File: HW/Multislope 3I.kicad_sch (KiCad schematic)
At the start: 126 parts, among them J1 INT, J10 PWR, J11 TEST, J12 UART, J13 INPUT, J14 SLOPE, J15 PWR, J2 TEST, J3 COMP, J4 SLOT, J5 SLOT, J6 SLOT, J7 SLOPE2, J8 PWR, J9 SLOT, SW1 RST, U1 OPA21xx, U10 LM311, U11 NE5534, U12 OPA197, U14 431, U15 MCP3202, U16 Pico, U17 LM35, U18 ADuM121N, U2 LM399, U20 HT7533, U21 HT7550, U3 CD4053B, U4 OPA1xx, U5 OPA1xx, U6 OPA1xx, U7 431, U8 431, U9 408

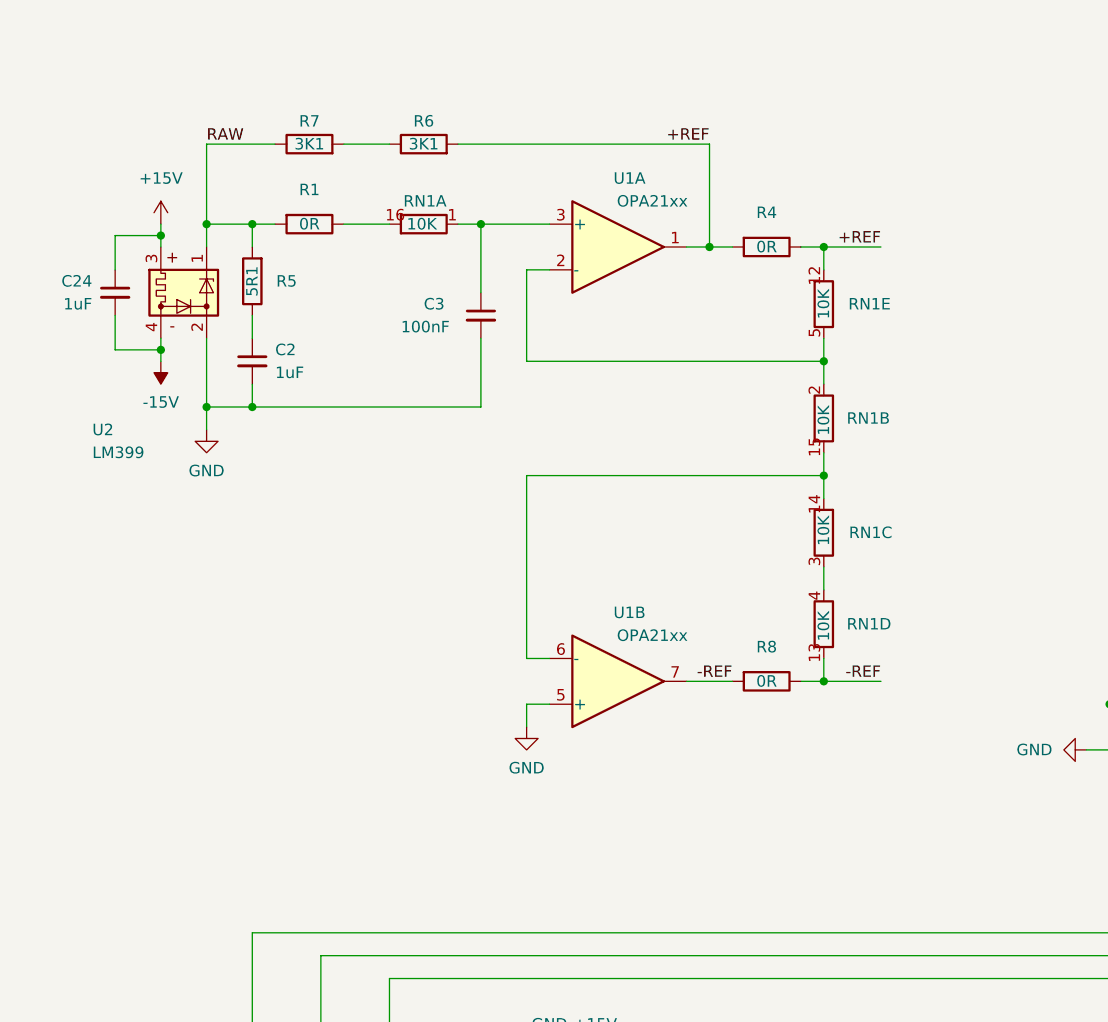
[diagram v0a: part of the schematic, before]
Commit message: Reference startup circuit added
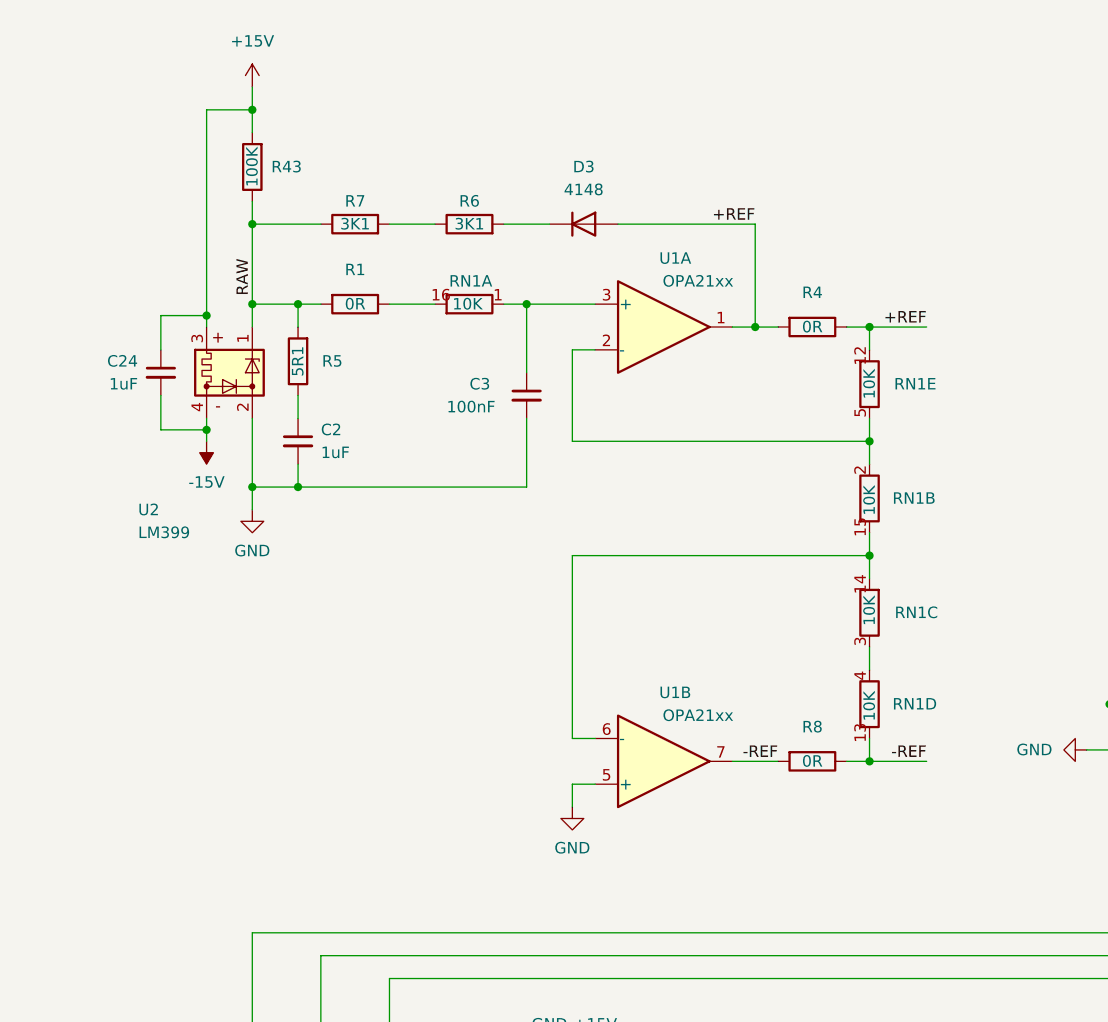
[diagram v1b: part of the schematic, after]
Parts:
- added D3: 4148, Diode_SMD:D_SOD-323, symbol Device:D
- added R43: 100K, Resistor_SMD:R_0603_1608Metric, symbol Device:R
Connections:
- net +15V: now also R43.2
- net +REF: now also D3.2 (A); no longer R6.2
- net RAW: now also R43.1
- new net: D3.1 (K), R6.2
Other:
- moved on the sheet: C2, C24, C3, R1, R4, R5, R6, R7, R8, RN1A, RN1B, RN1C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

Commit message: Schematic updated
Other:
- note added: "Unnecessary, oscillation on startup, not reliable Short footprint of D1/D2, DNP NE5534"
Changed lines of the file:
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@@
+    (stroke (width 0) (type default) (color 0 0 0 0))
+  )
+  (polyline (pts (xy 349.25 171.45) (xy 349.25 203.2))
     (stroke (width 0) (type default) (color 0 0 0 0))
   )
@@
     (stroke (width 0) (type default) (color 0 0 0 0))
   )
+  (polyline (pts (xy 347.98 171.45) (xy 349.25 171.45))
+    (stroke (width 0) (type default) (color 0 0 0 0))
+  )
   (wire (pts (xy 312.42 176.53) (xy 309.88 176.53))
     (stroke (width 0) (type default) (color 0 0 0 0))
@@
     (stroke (width 0) (type default) (color 0 0 0 0))
   )
+  (polyline (pts (xy 311.15 176.53) (xy 311.15 203.2))
+    (stroke (width 0) (type default) (color 0 0 0 0))
+  )
   (wire (pts (xy 248.92 111.76) (xy 248.92 114.3))
     (stroke (width 0) (type default) (color 0 0 0 0))
@@
     (stroke (width 0) (type default) (color 0 0 0 0))
   )
+  (polyline (pts (xy 349.25 203.2) (xy 311.15 203.2))
+    (stroke (width 0) (type default) (color 0 0 0 0))
+  )
   (wire (pts (xy 179.07 179.07) (xy 181.61 179.07))
     (stroke (width 0) (type default) (color 0 0 0 0))
@@
     (stroke (width 0) (type default) (color 0 0 0 0))
   )
+  (polyline (pts (xy 311.15 176.53) (xy 311.15 171.45))
+    (stroke (width 0) (type default) (color 0 0 0 0))
+  )
   (wire (pts (xy 397.51 134.62) (xy 389.89 134.62))
     (stroke (width 0) (type default) (color 0 0 0 0))
@@
   )
   (wire (pts (xy 104.14 261.62) (xy 109.22 261.62))
+    (stroke (width 0) (type default) (color 0 0 0 0))
+  )
+  (polyline (pts (xy 311.15 171.45) (xy 347.98 171.45))
     (stroke (width 0) (type default) (color 0 0 0 0))
   )
@@
     (effects (font (size 1.27 1.27)) (justify left bottom))
   )
+  (text "Unnecessary, oscillation on startup, not reliable\nShort footprint of D1/D2, DNP NE5534"
+    (at 311.15 208.28 0)
+    (effects (font (size 1.27 1.27)) (justify left bottom))
+  )

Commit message: Schematic updated
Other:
- note added: "Unreliable operation Do not populate R19/20 shorted/10R resistor"
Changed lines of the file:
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@@
+    (stroke (width 0) (type default) (color 0 0 0 0))
+  )
+  (polyline (pts (xy 132.08 209.55) (xy 119.38 209.55))
     (stroke (width 0) (type default) (color 0 0 0 0))
   )
@@
     (stroke (width 0) (type default) (color 0 0 0 0))
   )
+  (polyline (pts (xy 132.08 154.94) (xy 132.08 209.55))
+    (stroke (width 0) (type default) (color 0 0 0 0))
+  )
   (wire (pts (xy 147.32 125.73) (xy 140.97 125.73))
     (stroke (width 0) (type default) (color 0 0 0 0))
@@
     (stroke (width 0) (type default) (color 0 0 0 0))
   )
+  (polyline (pts (xy 119.38 184.15) (xy 119.38 154.94))
+    (stroke (width 0) (type default) (color 0 0 0 0))
+  )
   (wire (pts (xy 375.92 222.25) (xy 375.92 219.71))
     (stroke (width 0) (type default) (color 0 0 0 0))
@@
     (stroke (width 0) (type default) (color 0 0 0 0))
   )
+  (polyline (pts (xy 119.38 184.15) (xy 119.38 209.55))
+    (stroke (width 0) (type default) (color 0 0 0 0))
+  )
   (wire (pts (xy 279.4 233.68) (xy 281.94 233.68))
     (stroke (width 0) (type default) (color 0 0 0 0))
@@
   )
   (wire (pts (xy 52.07 262.89) (xy 52.07 261.62))
+    (stroke (width 0) (type default) (color 0 0 0 0))
+  )
+  (polyline (pts (xy 119.38 154.94) (xy 132.08 154.94))
     (stroke (width 0) (type default) (color 0 0 0 0))
   )
@@
     (effects (font (size 1.27 1.27)) (justify left bottom))
   )
+  (text "Unreliable operation\nDo not populate\nR19/20 shorted/10R resistor"
+    (at 119.38 215.9 0)
+    (effects (font (size 1.27 1.27)) (justify left bottom))
+  )

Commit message: Updated Schematic
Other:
- note added: "Note: +/-REF shouldn't be selected beacuse they saturate the integrator, consequence of having same integrator resistor values for input and references."
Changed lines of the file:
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@@
+    (effects (font (size 1.27 1.27)) (justify left bottom))
+  )
+  (text "Note:\n+/-REF shouldn't be selected beacuse they \nsaturate the integrator, consequence of \nhaving same integrator resistor values \nfor input and references."
+    (at 15.24 208.28 0)
     (effects (font (size 1.27 1.27)) (justify left bottom))
   )
